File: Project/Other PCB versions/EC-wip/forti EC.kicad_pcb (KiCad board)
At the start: 4 copper layers, 245.7 x 83.6 mm, 156 parts, among them J2 USB_C_Receptacle_USB2.0, SW1 BOOT0, U1 USBLC6-2SC6, U2 XC6206PxxxMR-Regulator_Linear, U4 74AHCT1G125, U5 74HC4051, U6 OPA350, U7 74HC4051, U8 STM32F401CBUx, Y1 8 MHz

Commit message: EC progress
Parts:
- removed C11: 220p, Capacitor_SMD:C_0402_1005Metric
- removed C14: 100n, Capacitor_SMD:C_0402_1005Metric
- removed the G*** at (40.7, 41.3)
- removed JP1: Ext_Res, Resistor_SMD:R_0603_1608Metric_Pad0.98x0.95mm_HandSolder
- removed R10: 1k, Resistor_SMD:R_0402_1005Metric
- removed R3: 100k, Resistor_SMD:R_0402_1005Metric
- removed SW_EC55, SW_EC58: 1.5u, cipulot_parts:ecs_pad_1U_no_ring
- removed U6: OPA350, Package_SO:SOIC-8_3.9x4.9mm_P1.27mm
- added C3: 100n, Capacitor_SMD:C_0402_1005Metric, B.Cu at (50.6, 63.3)
- added C4: 220pF NP0, Capacitor_SMD:C_0402_1005Metric, B.Cu at (55.7, 64.8)
- added R23: 1k, Resistor_SMD:R_0402_1005Metric, B.Cu at (50.6, 65.2)
- added R26: DNP, Resistor_SMD:R_0402_1005Metric, B.Cu at (54.0, 62.0)
- added R6: 100k, Resistor_SMD:R_0402_1005Metric, B.Cu at (54.0, 61.0)
- added U3: OPA354, Package_TO_SOT_SMD:SOT-23-5, B.Cu at (53.1, 64.3)
- G***: moved to F.Cu
- SW_EC38, SW_EC60, SW_EC61: footprint cipulot_parts:ecs_pad_1U_no_ring -> cipulot_parts:ecs_pad_1U_no_ring_1u_edge_cut
- SW_EC39, SW_EC45: footprint cipulot_parts:ecs_pad_1U_no_ring -> cipulot_parts:ecs_pad_no_ring_stepped&normal_cut
- moved G*** 104.4 mm to (247.7, 41.3)
- moved G*** 89.8 mm to (52.4, 41.3)
- moved G*** 55.4 mm to (190.5, 100.1), turned to 0 degrees
- moved C1 55.0 mm to (73.6, 50.8), turned to -90 degrees
- moved U2 51.9 mm to (70.6, 50.8), turned to 0 degrees
- moved C2 49.0 mm to (67.8, 50.8), turned to 90 degrees
- moved U4 47.5 mm to (37.3, 88.9), turned to -90 degrees
- moved C12 45.7 mm to (34.7, 89.4), turned to -90 degrees
- moved G*** 23.8 mm to (40.5, 41.3)
- moved R19 14.5 mm to (42.0, 52.6), turned to 180 degrees
- moved R21 11.9 mm to (42.0, 50.5), turned to 0 degrees
- moved R20 11.4 mm to (42.0, 51.6), turned to 180 degrees
- moved C19 10.6 mm to (61.2, 59.0), turned to -90 degrees
- moved C18 9.72 mm to (61.2, 49.8), turned to 90 degrees
- moved R24 9.45 mm to (49.2, 52.8), turned to -90 degrees
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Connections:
- R19 pad 1: Net-(U8-PB12) -> Net-(U8-PA3)
- R19 pad 2: ROW3 -> ROW1
- R20 pad 1: Net-(U8-PB13) -> Net-(U8-PA4)
- R20 pad 2: ROW0 -> ROW2
- R21 pad 1: ROW1 -> ROW3
- R21 pad 2: Net-(U8-PB14) -> Net-(U8-PA5)
- R22 pad 1: ROW2 -> ROW0
- R22 pad 2: Net-(U8-PB15) -> Net-(U8-PA6)
- SW_EC1 pad 1: ROW0 -> COL0
- SW_EC1 pad 2: COL0 -> ROW0
- SW_EC10 pad 1: ROW0 -> COL9
- SW_EC10 pad 2: COL9 -> ROW0
- SW_EC11 pad 1: ROW0 -> COL10
- SW_EC11 pad 2: COL10 -> ROW0
- SW_EC12 pad 1: ROW0 -> COL11
- SW_EC12 pad 2: COL11 -> ROW0
- SW_EC13 pad 1: ROW1 -> COL0
- SW_EC13 pad 2: COL0 -> ROW1
- SW_EC14 pad 1: ROW1 -> COL1
- SW_EC14 pad 2: COL1 -> ROW1
- SW_EC15 pad 1: ROW1 -> COL2
- SW_EC15 pad 2: COL2 -> ROW1
- SW_EC16 pad 1: ROW1 -> COL3
- SW_EC16 pad 2: COL3 -> ROW1
- SW_EC17 pad 1: ROW1 -> COL4
- SW_EC17 pad 2: COL4 -> ROW1
- SW_EC18 pad 1: ROW1 -> COL5
- SW_EC18 pad 2: COL5 -> ROW1
- SW_EC19 pad 1: ROW1 -> COL6
- SW_EC19 pad 2: COL6 -> ROW1
- SW_EC2 pad 1: ROW0 -> COL1
- SW_EC2 pad 2: COL1 -> ROW0
- SW_EC20 pad 1: ROW1 -> COL7
- SW_EC20 pad 2: COL7 -> ROW1
- SW_EC21 pad 1: ROW1 -> COL8
- SW_EC21 pad 2: COL8 -> ROW1
- SW_EC22 pad 1: ROW1 -> COL9
- SW_EC22 pad 2: COL9 -> ROW1
- SW_EC23 pad 1: ROW1 -> COL10
- SW_EC23 pad 2: COL10 -> ROW1
- SW_EC24 pad 1: ROW1 -> COL11
- SW_EC24 pad 2: COL11 -> ROW1
- SW_EC25 pad 1: ROW2 -> COL0
- SW_EC25 pad 2: COL0 -> ROW2
- SW_EC26 pad 1: ROW2 -> COL1
- SW_EC26 pad 2: COL1 -> ROW2
- SW_EC27 pad 1: ROW2 -> COL2
- SW_EC27 pad 2: COL2 -> ROW2
- SW_EC28 pad 1: ROW2 -> COL3
- SW_EC28 pad 2: COL3 -> ROW2
- SW_EC29 pad 1: ROW2 -> COL4
- SW_EC29 pad 2: COL4 -> ROW2
- SW_EC3 pad 1: ROW0 -> COL2
- SW_EC3 pad 2: COL2 -> ROW0
- SW_EC30 pad 1: ROW2 -> COL5
- SW_EC30 pad 2: COL5 -> ROW2
- SW_EC31 pad 1: ROW2 -> COL6
- SW_EC31 pad 2: COL6 -> ROW2
- SW_EC32 pad 1: ROW2 -> COL7
- SW_EC32 pad 2: COL7 -> ROW2
- SW_EC33 pad 1: ROW2 -> COL8
- SW_EC33 pad 2: COL8 -> ROW2
- SW_EC34 pad 1: ROW2 -> COL9
- SW_EC34 pad 2: COL9 -> ROW2
- SW_EC35 pad 3: GND -> ROW2
- SW_EC35 pad 4: (no net) -> GND
- SW_EC36 pad 3: GND -> ROW2
- SW_EC36 pad 4: (no net) -> GND
- SW_EC37 pad 1: ROW3 -> COL0
- SW_EC37 pad 2: COL0 -> ROW3
- SW_EC38 pad 1: ROW3 -> COL1
- SW_EC38 pad 2: COL1 -> ROW3
- SW_EC39 pad 1: ROW3 -> COL2
- SW_EC39 pad 2: COL2 -> ROW3
- SW_EC4 pad 1: ROW0 -> COL3
- SW_EC4 pad 2: COL3 -> ROW0
- SW_EC40 pad 1: ROW3 -> COL3
- SW_EC40 pad 2: COL3 -> ROW3
- SW_EC41 pad 1: ROW3 -> COL4
- SW_EC41 pad 2: COL4 -> ROW3
- SW_EC42 pad 1: ROW3 -> COL6
- SW_EC42 pad 2: COL5 -> ROW3
- SW_EC43 pad 1: ROW3 -> COL7
- SW_EC43 pad 2: COL6 -> ROW3
- SW_EC44 pad 1: ROW3 -> COL8
- SW_EC44 pad 2: COL7 -> ROW3
- SW_EC45 pad 2: COL8 -> COL9
- SW_EC46 pad 1: ROW3 -> COL10
- SW_EC46 pad 2: COL9 -> ROW3
- SW_EC47 pad 1: ROW3 -> COL11
- SW_EC47 pad 2: COL10 -> ROW3
- SW_EC48 pad 1: ROW1 -> COL11
- SW_EC48 pad 2: COL11 -> ROW1
- SW_EC49 pad 1: ROW1 -> COL11
- SW_EC49 pad 2: COL11 -> ROW1
- SW_EC5 pad 1: ROW0 -> COL4
- SW_EC5 pad 2: COL4 -> ROW0
- SW_EC50 pad 1: ROW2 -> COL0
- SW_EC50 pad 2: COL0 -> ROW2
- SW_EC6 pad 1: ROW0 -> COL5
- SW_EC6 pad 2: COL5 -> ROW0
- SW_EC60 pad 2: COL9 -> COL10
- SW_EC61 pad 1: ROW3 -> COL1
- SW_EC61 pad 2: COL1 -> ROW3
- SW_EC7 pad 1: ROW0 -> COL6
- SW_EC7 pad 2: COL6 -> ROW0
- SW_EC8 pad 1: ROW0 -> COL7
- SW_EC8 pad 2: COL7 -> ROW0
- SW_EC9 pad 1: ROW0 -> COL8
- SW_EC9 pad 2: COL8 -> ROW0
- U8 pad 12: unconnected-(U8-PA2-Pad12) -> RGB MCU
- U8 pad 13: ADC -> Net-(U8-PA3)
- U8 pad 14: APLEX_OUT_PIN_0 -> Net-(U8-PA4)
- U8 pad 15: unconnected-(U8-PA5-Pad15) -> Net-(U8-PA5)
- U8 pad 16: unconnected-(U8-PA6-Pad16) -> Net-(U8-PA6)
- U8 pad 18: APLEX_EN_PIN_0 -> unconnected-(U8-PB0-Pad18)
- U8 pad 19: APLEX_EN_PIN_1 -> unconnected-(U8-PB1-Pad19)
- U8 pad 25: Net-(U8-PB12) -> unconnected-(U8-PB12-Pad25)
- U8 pad 26: Net-(U8-PB13) -> unconnected-(U8-PB13-Pad26)
- U8 pad 27: Net-(U8-PB14) -> unconnected-(U8-PB14-Pad27)
- U8 pad 28: Net-(U8-PB15) -> unconnected-(U8-PB15-Pad28)
- U8 pad 34: SWDIO -> unconnected-(U8-PA13-Pad34)
- U8 pad 37: SWCLK -> AMUX_SEL_2
- U8 pad 38: unconnected-(U8-PA15-Pad38) -> AMUX_SEL_1
- U8 pad 39: AMUX_SEL_2 -> AMUX_SEL_0
- U8 pad 40: AMUX_SEL_1 -> APLEX_EN_PIN_1
- U8 pad 41: AMUX_SEL_0 -> APLEX_EN_PIN_0
- U8 pad 42: unconnected-(U8-PB6-Pad42) -> APLEX_OUT_PIN_0
- U8 pad 43: unconnected-(U8-PB7-Pad43) -> ADC
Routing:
- net AMUX_SEL_0: track 0.00 -> 235.4 mm, vias 0 -> 2
- net AMUX_SEL_1: track 0.00 -> 235.1 mm, vias 0 -> 2
- net AMUX_SEL_2: track 0.00 -> 235.1 mm, vias 0 -> 2
- net VBAT: track 46.8 -> 254.1 mm, vias 4 -> 8
- net APLEX_OUT_PIN_0: track 2.08 -> 186.8 mm, vias 0 -> 3
- net APLEX_EN_PIN_1: track 0.00 -> 178.6 mm, vias 0 -> 2
- net COL11: track 5.50 -> 165.6 mm, vias 6 -> 8
- net ROW3: track 307.9 -> 459.3 mm, vias 26 -> 22
- net COL10: track 12.3 -> 151.2 mm, vias 6 -> 7
- net COL1: track 0.00 -> 130.7 mm, vias 4 -> 5
- net ROW2: track 321.3 -> 441.0 mm, vias 14 -> 17
- net COL2: track 0.00 -> 111.2 mm, vias 6 -> 5
- net COL9: track 8.22 -> 118.0 mm, vias 4 -> 5
- net COL0: track 68.6 -> 169.0 mm
- net +5V: track 469.4 -> 568.2 mm, vias 16 -> 21
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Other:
- board text added: "ADD EDGE CUT to 4.1"
- board text added: "EC"
- board text added: "boot"

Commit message: progress on EC version
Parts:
- SW_EC23, SW_EC49: footprint cipulot_parts:ecs_pad_1U_no_ring -> cipulot_parts:ecs_pad_1U_no_ring_1u_edge_cut
- moved H1 230.4 mm to (31.0, 41.3)
- moved H2 192.0 mm to (73.8, 41.3)
- moved H9 186.9 mm to (69.1, 79.4)
- moved H6 167.8 mm to (97.6, 60.3)
- moved H3 144.2 mm to (131.0, 41.3)
- moved H12 140.7 mm to (114.3, 98.4)
- moved H10 133.1 mm to (126.2, 79.4)
- moved H7 107.8 mm to (173.8, 60.3)
- moved H4 96.9 mm to (207.2, 41.3)
- moved H13 96.4 mm to (161.9, 98.4)
- moved H5 94.2 mm to (270.7, 41.3)
- moved H22 75.6 mm to (181.8, 125.3)
- moved H24 75.6 mm to (181.8, 131.7)
- moved H25 75.6 mm to (181.8, 134.9)
- moved H23 75.6 mm to (181.8, 128.5)
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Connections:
- SW_EC23 pad 1: COL10 -> ROW1
- SW_EC23 pad 2: ROW1 -> COL10
- SW_EC36 pad 1: ROW2 -> COL11
- SW_EC36 pad 2: COL11 -> ROW2
- SW_EC36 pad 3: ROW2 -> COL11
- SW_EC52 pad 2: COL10 -> COL11
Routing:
- net COL11: track 165.6 -> 205.4 mm, vias 8 -> 9
- net ROW1: track 409.7 -> 393.3 mm
- net ROW2: track 441.0 -> 425.8 mm
- net ROW3: track 459.3 -> 453.0 mm
- net ROW0: track 346.0 -> 350.0 mm
- net +5V: track 568.2 -> 566.8 mm
- net COL10: track 151.2 -> 152.5 mm, vias 7 -> 6
- net GND: vias 256 -> 258
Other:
- board text added: "MOUNTING HOLES!!! OVERLAP CHECK3"

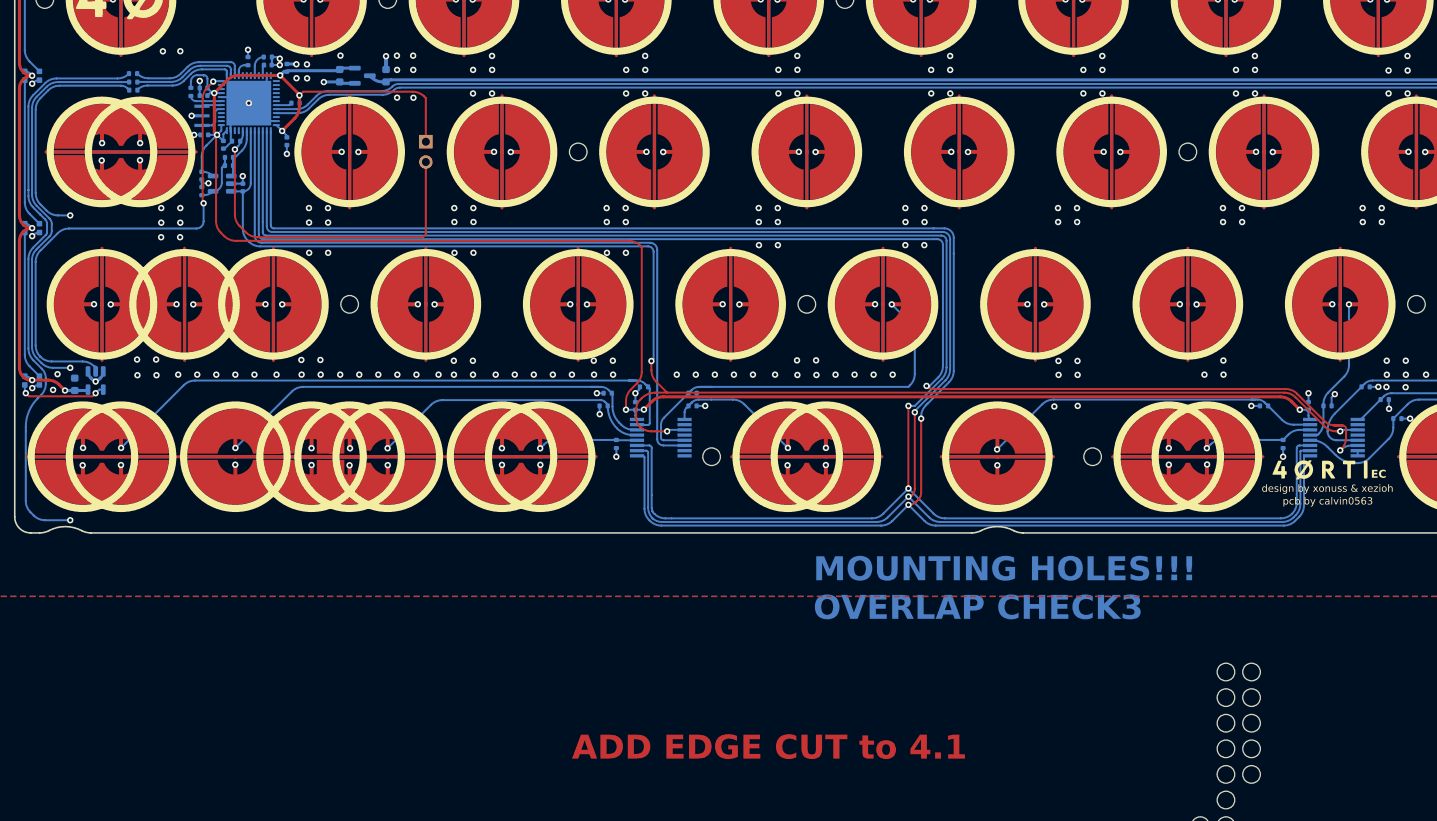
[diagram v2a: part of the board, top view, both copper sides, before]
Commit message: small changes made after left shift was discovered to be wrong
new new edge cut for full revision though
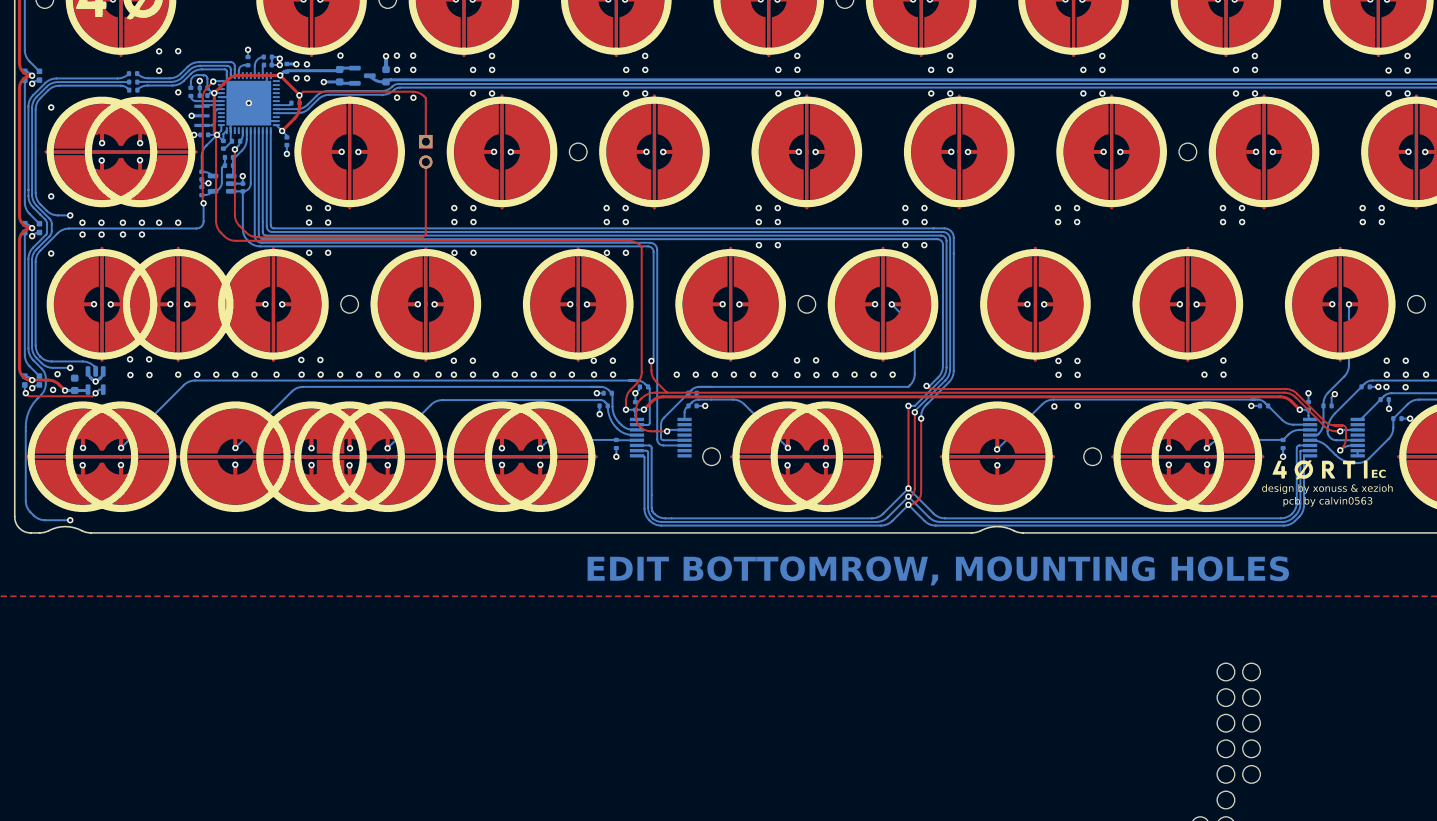
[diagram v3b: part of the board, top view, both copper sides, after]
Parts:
- moved SW_EC50 0.79 mm to (47.6, 79.4)
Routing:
- net COL0: track 169.0 -> 187.2 mm
- net ROW2: track 425.8 -> 426.5 mm
- net GND: vias 258 -> 267
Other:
- board text added: "EDIT BOTTOMROW, MOUNTING HOLES"
- board text removed: "ADD EDGE CUT to 4.1"
- board text removed: "MOUNTING HOLES!!! OVERLAP CHECK3"
